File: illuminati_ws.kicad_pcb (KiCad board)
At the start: 2 copper layers, 75.5 x 63.5 mm, 55 parts, among them IC1 ESP32-C3-WROOM-02-N4, J1 Conn_02x03_Odd_Even, J10 Conn_01x03, J11 Conn_01x03, J14 Conn_01x04, J2 Conn_01x03, J3 Conn_01x03, J4 Conn_01x03, J5 Conn_01x03, J7 Conn_01x03, J8 Conn_01x03, J9 Conn_01x03, SW1 SW_SPST, U2 74HC14, U3 74HC14, U4 74HC14, U6 AMS1117-3.3

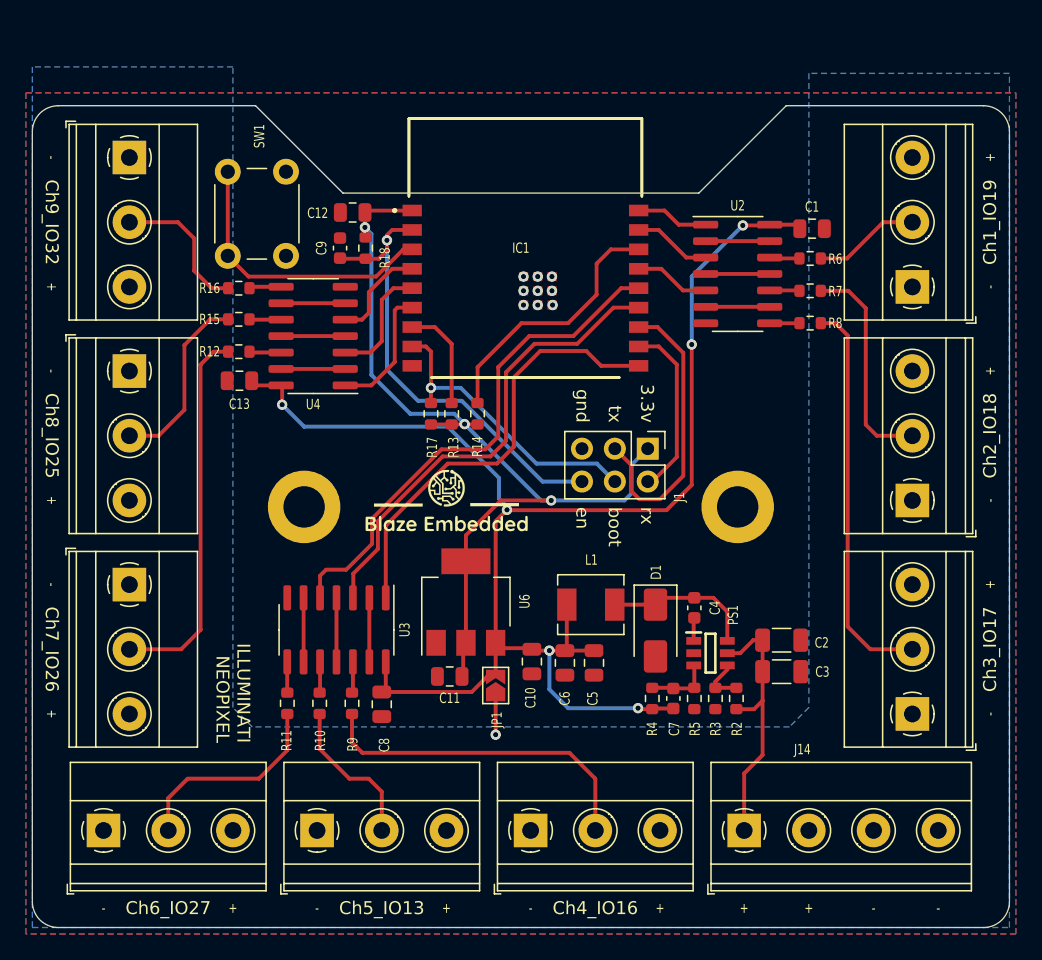
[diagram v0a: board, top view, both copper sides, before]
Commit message: Board V2 swap esp32c3 for esp32
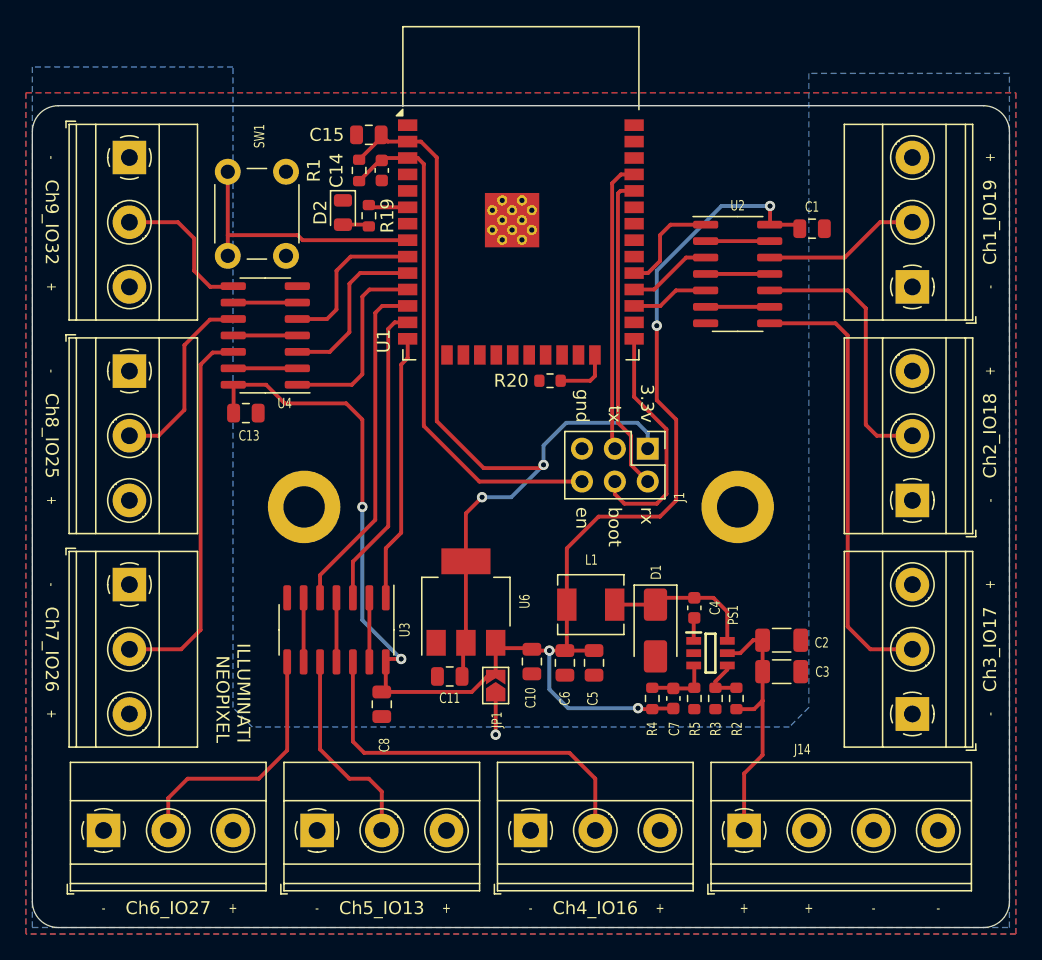
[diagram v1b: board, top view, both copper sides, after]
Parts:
- removed C12: 22u, Capacitor_SMD:C_0805_2012Metric
- removed C9: 100n, Capacitor_SMD:C_0603_1608Metric
- removed the G*** at (144.0, 114.5)
- removed IC1: ESP32-C3-WROOM-02-N4, SamacSys_Parts:ESP32C3WROOM02N4
- removed R10, R11, R12, R15, R16, R6, R7, R8, R9: 330R, Resistor_SMD:R_0603_1608Metric
- removed R13, R14, R17, R18: 10k, Resistor_SMD:R_0603_1608Metric
- added C14: 100n, Capacitor_SMD:C_0603_1608Metric, F.Cu at (139.0, 89.0)
- added C15: 22u, Capacitor_SMD:C_0805_2012Metric, F.Cu at (138.0, 86.2)
- added D2: LED, LED_SMD:LED_0805_2012Metric, F.Cu at (136.0, 92.2)
- added R1: 10k, Resistor_SMD:R_0603_1608Metric, F.Cu at (137.2, 89.0)
- added R19: 2k, Resistor_SMD:R_0603_1608Metric, F.Cu at (138.0, 92.5)
- added R20: 10k, Resistor_SMD:R_0603_1608Metric, F.Cu at (152.0, 105.2)
- added U1: ESP32-WROOM-32, RF_Module:ESP32-WROOM-32, F.Cu at (149.8, 93.8)
- moved U4 3.70 mm to (130.0, 101.8)
- moved C13 2.55 mm to (128.5, 107.8), turned to 0 degrees
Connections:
- SW1 pad 1: /sw -> /btn
- U2 pad 10: Net-(R7-Pad1) -> Net-(J4-Pin_2)
- U2 pad 12: Net-(R6-Pad1) -> Net-(J3-Pin_2)
- U2 pad 8: Net-(R8-Pad1) -> Net-(J5-Pin_2)
- U3 pad 10: Net-(R10-Pad1) -> Net-(J7-Pin_2)
- U3 pad 12: Net-(R9-Pad1) -> Net-(J2-Pin_2)
- U3 pad 8: Net-(R11-Pad1) -> Net-(J8-Pin_2)
- U4 pad 10: Net-(R15-Pad1) -> Net-(J10-Pin_2)
- U4 pad 12: Net-(R12-Pad1) -> Net-(J9-Pin_2)
- U4 pad 8: Net-(R16-Pad1) -> Net-(J11-Pin_2)
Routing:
- net /sw: track 22.3 -> 0.00 mm
- net /btn: track 0.00 -> 20.6 mm
- net /gpio2: track 20.4 -> 0.00 mm
- net /neopixel4: track 34.3 -> 20.7 mm
- net /neopixel6: track 39.8 -> 26.5 mm
- net /neopixel5: track 36.8 -> 23.6 mm
- net /rx: track 13.7 -> 24.5 mm
- net /gpio8: track 8.16 -> 0.00 mm
- net /neopixel7: track 10.0 -> 15.1 mm
- net /neopixel9: track 7.74 -> 12.3 mm
- net Net-(U1-IO2): track 0.00 -> 4.42 mm
- net /esp_en: track 35.9 -> 40.2 mm, vias 1 -> 0
- net /boot: track 22.8 -> 18.6 mm, vias 1 -> 0
- net /neopixel8: track 9.11 -> 13.2 mm
- net Net-(J8-Pin_2): track 16.0 -> 20.1 mm
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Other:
- outline, holes or cut-outs redrawn
